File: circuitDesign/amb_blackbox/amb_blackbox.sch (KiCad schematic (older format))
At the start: 9 parts, among them P1 CONN_2

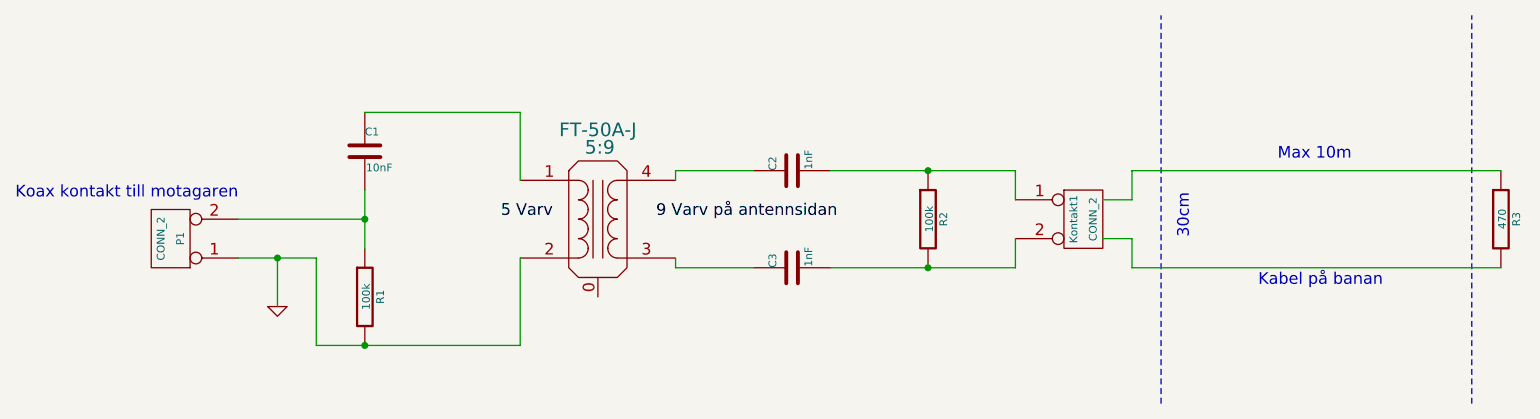
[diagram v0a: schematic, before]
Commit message: Updated blackbox with working and tested design
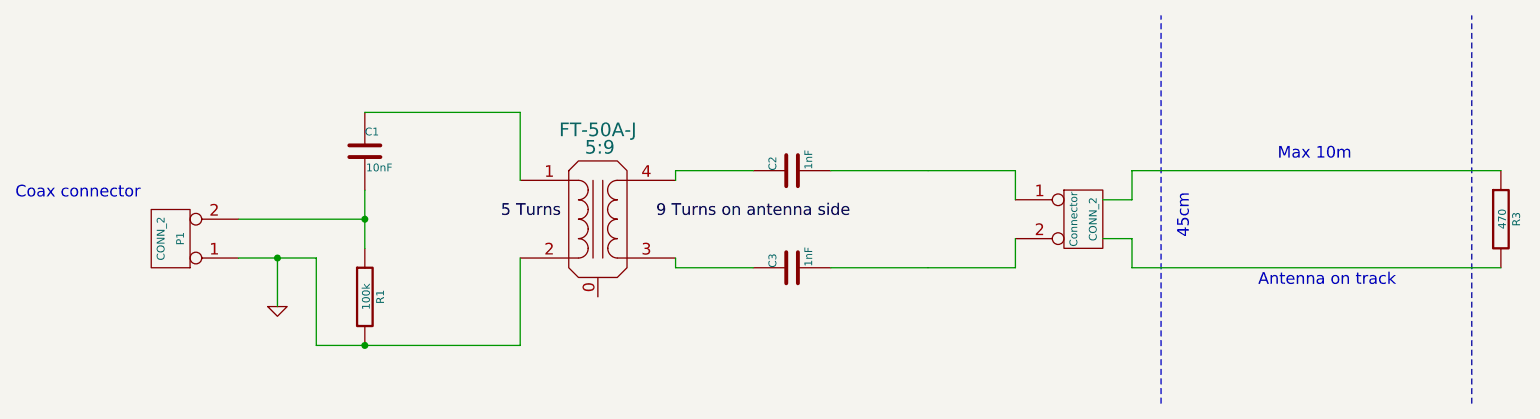
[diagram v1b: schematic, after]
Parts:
- removed R2: 100k, ~, symbol R
- renumbered Kontakt1 to Connector
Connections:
- net labels added: 5 Turns, 9 Turns on antenna side
- net labels removed: 5 Varv, 9 Varv på antennsidan
- wire segments 23 -> 28
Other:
- note added: "45cm"
- note added: "Antenna on track"
- note added: "Coax connector"
- note removed: "30cm"
- note removed: "Kabel på banan"
- note removed: "Koax kontakt till motagaren"
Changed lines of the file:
@@
 LIBS:contrib
 LIBS:valves
+LIBS:amb_blackbox-cache
 EELAYER 27 0
 EELAYER END
@@
 Sheet 1 1
 Title ""
-Date "5 may 2015"
+Date "14 may 2018"
 Rev ""
 Comp ""
@@
 $EndDescr
 $Comp
-L CONN_2 Kontakt1
+L CONN_2 Connector
 U 1 1 55487760
 P 6700 3650
-F 0 "Kontakt1" V 6650 3650 40  0000 C CNN
+F 0 "Connector" V 6650 3650 40  0000 C CNN
 F 1 "CONN_2" V 6750 3650 40  0000 C CNN
 F 2 "~" H 6700 3650 60  0000 C CNN
@@
 $EndComp
 Wire Wire Line
-	2350 3850 2750 3850
+	2350 3850 2550 3850
+Wire Wire Line
+	2550 3850 2750 3850
 Wire Wire Line
 	2550 3850 2550 4100
@@
 $EndComp
 Wire Wire Line
-	3000 3500 3000 3800
+	3000 3500 3000 3650
+Wire Wire Line
+	3000 3650 3000 3800
 $Comp
 L C C1
@@
 $EndComp
 Text Label 4500 3650 0    60   ~ 0
-9 Varv på antennsidan
+9 Turns on antenna side
 Text Label 3700 3650 0    60   ~ 0
-5 Varv
+5 Turns
 Connection ~ 3000 3650
 Wire Wire Line
@@
 	3800 4300 3800 3850
 Wire Wire Line
-	2750 4300 3800 4300
+	2750 4300 3000 4300
+Wire Wire Line
+	3000 4300 3800 4300
 Wire Wire Line
 	2750 3850 2750 4300
@@
 	0    -1   -1   0
 $EndComp
-$Comp
-L R R2
-U 1 1 55487E43
-P 5900 3650
-F 0 "R2" V 5980 3650 40  0000 C CNN
-F 1 "100k" V 5907 3651 40  0000 C CNN
-F 2 "~" V 5830 3650 30  0000 C CNN
-F 3 "~" H 5900 3650 30  0000 C CNN
-	1    5900 3650
-	1    0    0    -1
-$EndComp
 Wire Wire Line
-	6350 3400 6350 3550
+	5400 3900 5900 3900
 Wire Wire Line
-	5400 3400 6350 3400
-Wire Wire Line
-	5400 3900 6350 3900
+	5900 3900 6350 3900
 Wire Wire Line
 	6350 3900 6350 3750
-Connection ~ 5900 3400
-Connection ~ 5900 3900
 Wire Wire Line
 	5000 3900 4600 3900
@@
 	8700 4600 8700 2600
 Text Notes 7600 4000 0    60   ~ 0
-Kabel på banan
+Antenna on track
 Text Notes 7250 3750 1    60   ~ 0
-30cm
+45cm
 Text Notes 1200 3550 0    60   ~ 0
-Koax kontakt till motagaren
+Coax connector
+Wire Wire Line
+	6350 3400 6350 3550
+Wire Wire Line
+	5400 3400 5900 3400
+Wire Wire Line
+	5900 3400 6350 3400
 $EndSCHEMATC
